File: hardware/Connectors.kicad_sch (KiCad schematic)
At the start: 18 parts, among them J1 USB_C_Receptacle_USB2.0, J14 Conn_01x05, J2 M80-5302642, J3 M300-MV31045M1, J4 M80-5L10442MC, J5 M80-5L10442MC, J6 M80-5L10442MC

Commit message: board sync
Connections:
- net HV_ACU+: no longer J5.4
- net HV_ACU-: no longer J5.1
- net HV_CAR+: no longer J4.4
- net HV_CAR-: no longer J4.1
- no-connect marks 2 -> 6
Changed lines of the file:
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@@
   (junction (at 121.92 136.525) (diameter 0) (color 0 0 0 0)
   )
+  (no_connect (at 187.96 41.275))
+  (no_connect (at 170.18 73.025))
+  (no_connect (at 170.18 43.815))
   (no_connect (at 263.525 66.675))
   (no_connect (at 263.525 69.215))
+  (no_connect (at 187.96 70.485))
   (wire (pts (xy 121.92 142.875) (xy 121.92 145.415))
     (stroke (width 0) (type default) (color 0 0 0 0))
@@
   )
   (wire (pts (xy 260.985 66.675) (xy 263.525 66.675))
-    (stroke (width 0) (type default) (color 0 0 0 0))
-  )
-  (wire (pts (xy 185.42 70.485) (xy 187.96 70.485))
     (stroke (width 0) (type default) (color 0 0 0 0))
   )
@@
     (stroke (width 0) (type default) (color 0 0 0 0))
   )
+  (wire (pts (xy 170.18 73.025) (xy 172.72 73.025))
+    (stroke (width 0) (type default) (color 0 0 0 0))
+  )
   (wire (pts (xy 268.605 43.815) (xy 268.605 46.355))
     (stroke (width 0) (type default) (color 0 0 0 0))
@@
   )
   (wire (pts (xy 81.915 80.01) (xy 79.375 80.01))
+    (stroke (width 0) (type default) (color 0 0 0 0))
+  )
+  (wire (pts (xy 185.42 70.485) (xy 187.96 70.485))
     (stroke (width 0) (type default) (color 0 0 0 0))
   )
@@
     (stroke (width 0) (type default) (color 0 0 0 0))
   )
-  (wire (pts (xy 172.72 73.025) (xy 170.18 73.025))
-    (stroke (width 0) (type default) (color 0 0 0 0))
-  )
   (wire (pts (xy 260.985 56.515) (xy 262.255 56.515))
     (stroke (width 0) (type default) (color 0 0 0 0))
@@
     )
   )
-  (global_label "HV_CAR+" (shape input) (at 170.18 43.815 180) (fields_autoplaced)
-    (effects (font (size 1.27 1.27)) (justify right))
-    (property "Intersheet References" "${INTERSHEET_REFS}" (id 0) (at 159.2682 43.7356 0)
-      (effects (font (size 1.27 1.27)) (justify right) hide)
-    )
-  )
   (global_label "IMD_SENSENSOR" (shape input) (at 53.975 97.155 180) (fields_autoplaced)
     (effects (font (size 1.27 1.27)) (justify right))
@@
     )
   )
-  (global_label "HV_ACU-" (shape input) (at 187.96 70.485 0) (fields_autoplaced)
-    (effects (font (size 1.27 1.27)) (justify left))
-    (property "Intersheet References" "${INTERSHEET_REFS}" (id 0) (at 198.9323 70.4056 0)
-      (effects (font (size 1.27 1.27)) (justify left) hide)
-    )
-  )
   (global_label "AIR_M_DETECTION" (shape input) (at 53.975 104.775 180) (fields_autoplaced)
     (effects (font (size 1.27 1.27)) (justify right))
@@
     )
   )
-  (global_label "HV_CAR-" (shape input) (at 187.96 41.275 0) (fields_autoplaced)
-    (effects (font (size 1.27 1.27)) (justify left))
-    (property "Intersheet References" "${INTERSHEET_REFS}" (id 0) (at 198.8718 41.1956 0)
-      (effects (font (size 1.27 1.27)) (justify left) hide)
-    )
-  )
   (global_label "D-" (shape input) (at 238.125 130.81 180) (fields_autoplaced)
     (effects (font (size 1.27 1.27)) (justify right))
@@
       (effects (font (size 1.27 1.27)) (justify right) hide)
     )
-  )
-  (global_label "HV_ACU+" (shape input) (at 170.18 73.025 180) (fields_autoplaced)
-    (effects (font (size 1.27 1.27)) (justify right))
-    (property "Intersheet References" "${INTERSHEET_REFS}" (id 0) (at 159.2077 72.9456 0)
-      (effects (font (size 1.27 1.27)) (justify right) hide)
-    )

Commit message: pcb iter 4?
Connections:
- net AIR_M+: now also J3.1, J3.2, J3.4, J3.5, J3.7, J3.8
- net AIR_M-: now also J3.6
- net AIR_M_DETECTION: now also J2.11
- net AIR_P-: now also J3.9
- net AIR_PRE-: now also J3.10
- net AIR_PRE_DETECTION: now also J2.10
- net AIR_P_DETECTION: now also J2.24
- net CAN_H: now also J2.17
- net CAN_L: now also J2.18
- net CUR_SENS_REF: now also J2.4
- net CUR_SENS_SIG: now also J2.5
- net DIN_1: now also J2.21
- net DIN_2: now also J2.22
- net DIN_3: now also J2.20
- net EXT_RESET: now also J2.19
- net GND: now also J2.15, J2.2, J3.3; no longer J2.14
- net IMD_SENSENSOR: now also J2.23
- net LTC_1_CHASSIS: now also J2.16
- net LTC_1_OUT_I+: now also J2.6
- net LTC_1_OUT_I-: now also J2.7
- net LTC_2_CHASSIS: now also J2.3
- net LTC_2_OUT_I+: now also J2.8
- net LTC_2_OUT_I-: now also J2.9
- net VDD: now also J2.14
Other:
- moved on the sheet: J3

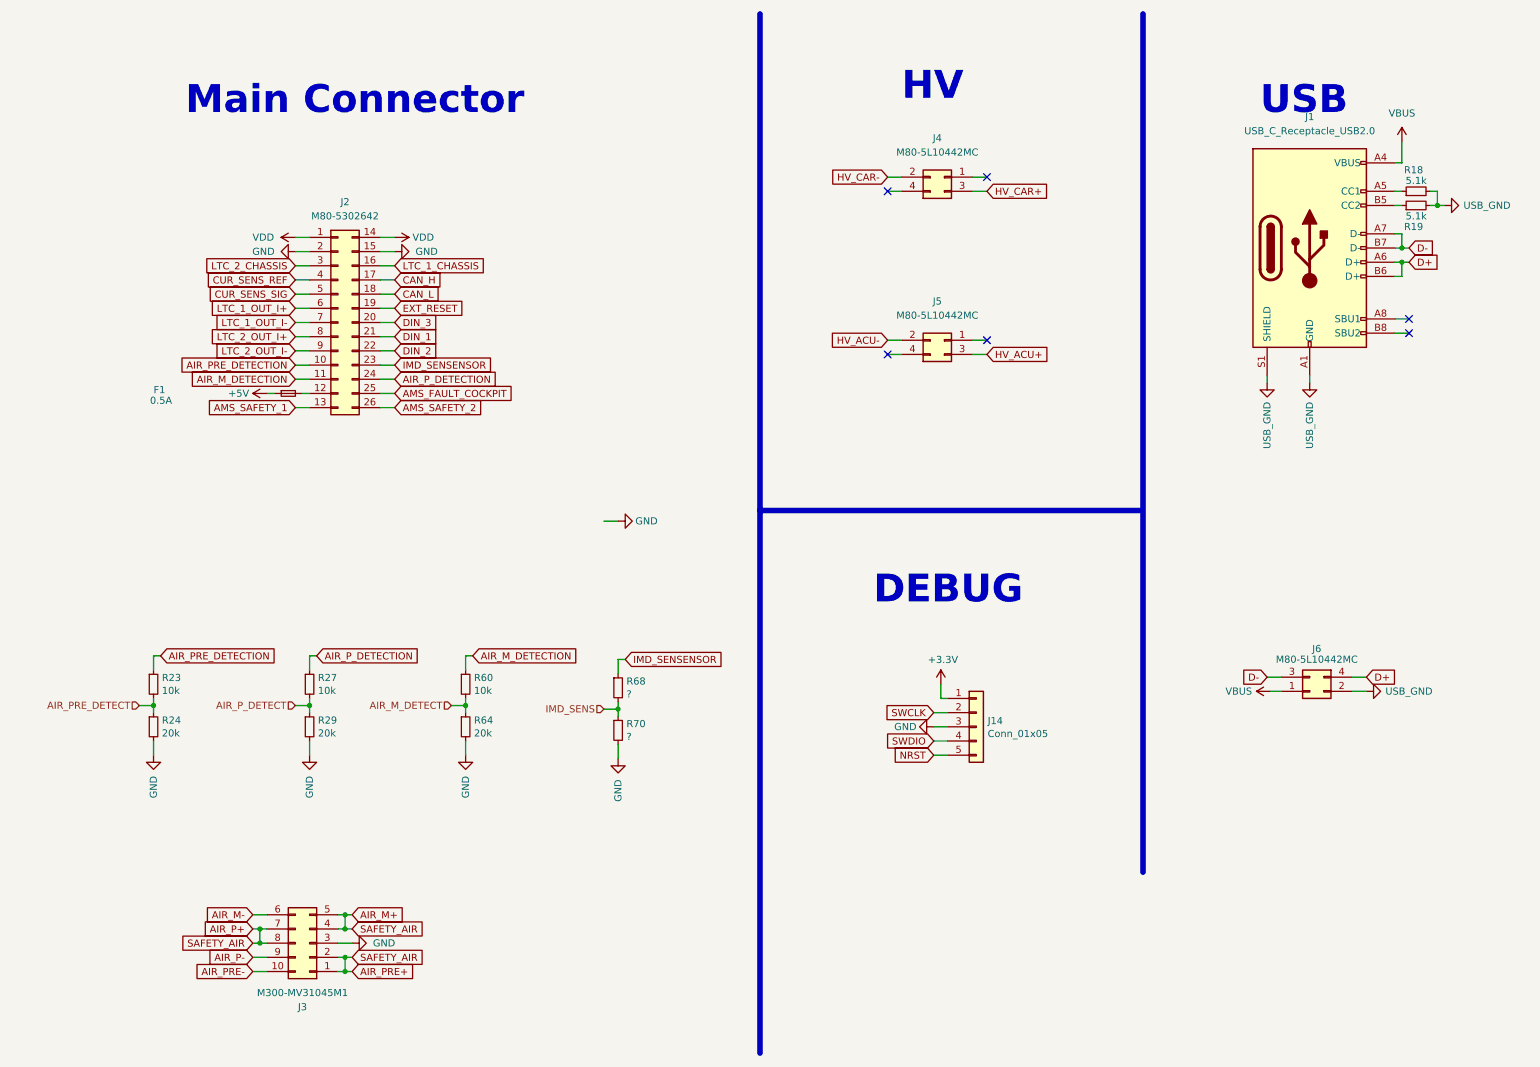
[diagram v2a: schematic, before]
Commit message: board layout changes, moved USB from seprate connector to the main connector, moved optos to the bootom right corner, moved IMD signal and air detection to a seprate connector
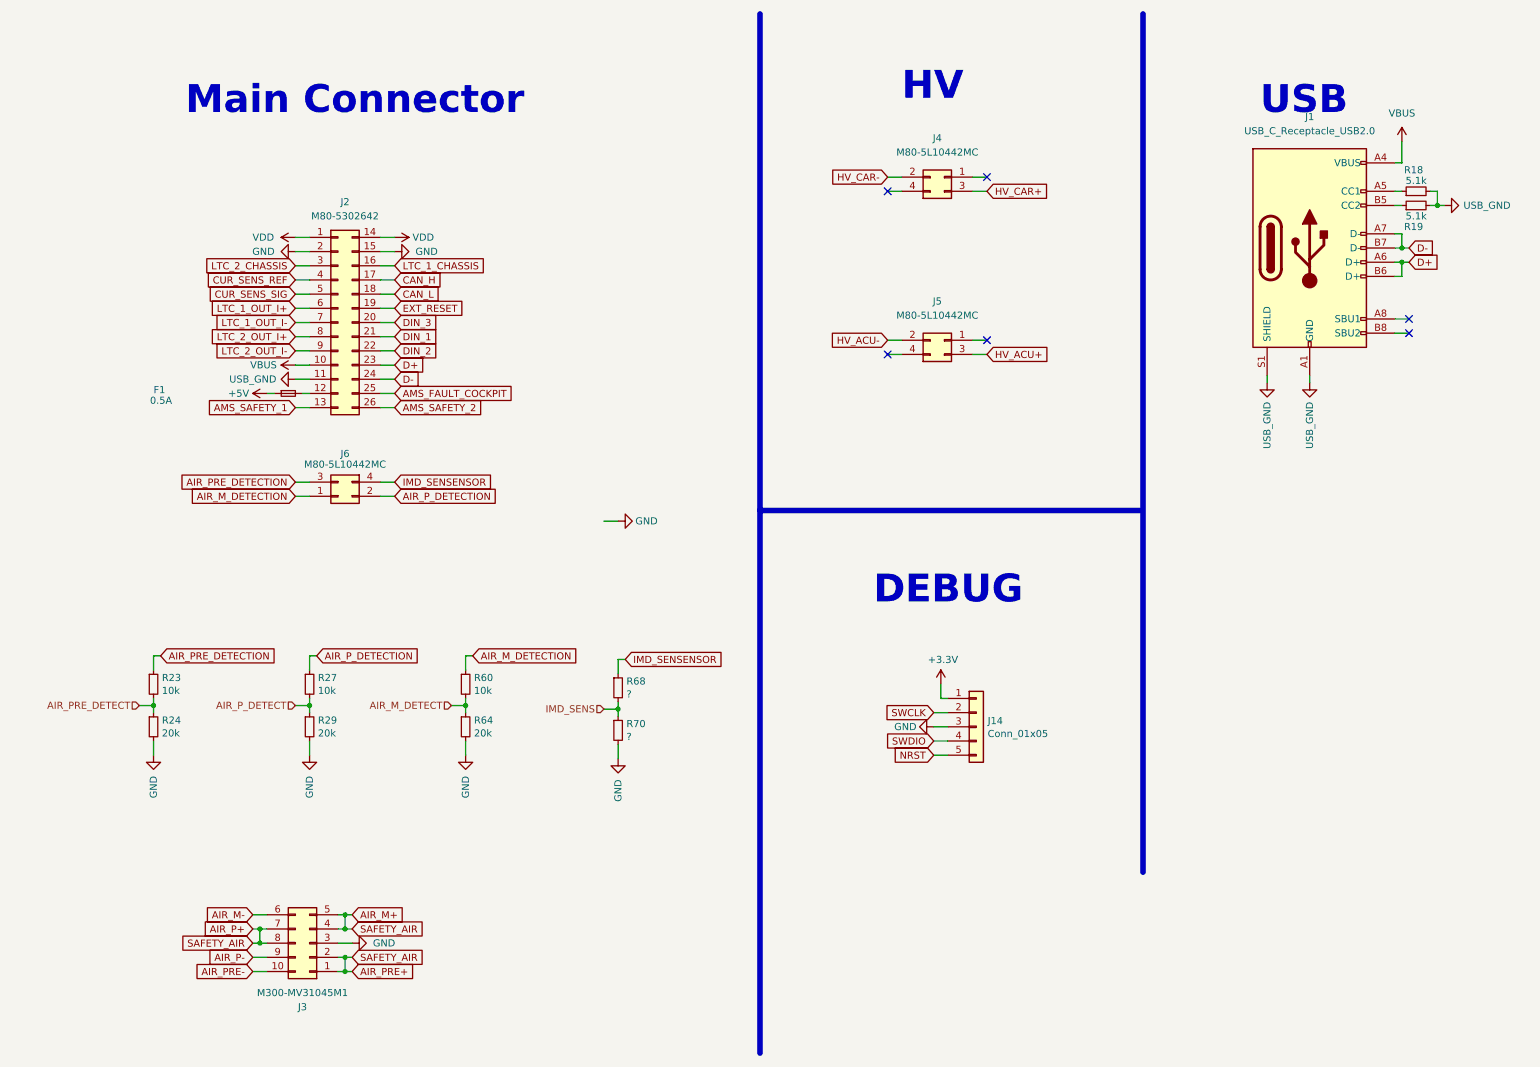
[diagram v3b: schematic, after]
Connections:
- net AIR_M_DETECTION: now also J6.1; no longer J2.11
- net AIR_PRE_DETECTION: now also J6.3; no longer J2.10
- net AIR_P_DETECTION: now also J6.2; no longer J2.24
- net D+: now also J2.23; no longer J6.4
- net D-: now also J2.24; no longer J6.3
- net IMD_SENSENSOR: now also J6.4; no longer J2.23
- net USB_GND: now also J2.11; no longer J6.2
- net VBUS: now also J2.10; no longer J6.1
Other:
- moved on the sheet: J6

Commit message: remake in progress
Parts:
- added D14, D15, D16, D17: 3.3V, Diode_SMD:D_SOD-323_HandSoldering, symbol Device:D_Zener_Small
- added J7: M80-5L10442MC, M80-5L104YYMC, symbol M80-5L10442MC:M80-5L10442MC
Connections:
- net AIR_M_DETECT: now also D16.1 (K)
- net AIR_PRE_DETECT: now also D14.1 (K)
- net AIR_P_DETECT: now also D15.1 (K)
- net GND: now also D14.2 (A), D15.2 (A), D16.2 (A), D17.2 (A)
- net IMD_SENS: now also D17.1 (K)
- net LTC_1_OUT_I+: now also J7.3; no longer J2.6
- net LTC_1_OUT_I-: now also J7.1; no longer J2.7
- net LTC_2_OUT_I+: now also J7.2; no longer J2.8
- net LTC_2_OUT_I-: now also J7.4; no longer J2.9
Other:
- moved on the sheet: F1, J1, J14, J2, J3, J4, J5, J6, R18, R19, R23, R24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
